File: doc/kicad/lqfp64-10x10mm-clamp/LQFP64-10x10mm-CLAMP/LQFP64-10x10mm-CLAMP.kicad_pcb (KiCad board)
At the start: 2 copper layers, 50 x 25 mm, 11 parts, among them J0 Conn_01x01, J1 Conn_01x16, J2 Conn_01x16, J3 Conn_01x16, J4 Conn_01x16, J5 Conn_01x12, J6 Conn_01x12, J7 Conn_01x12, J8 Conn_01x12, U1 LQFP64-G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

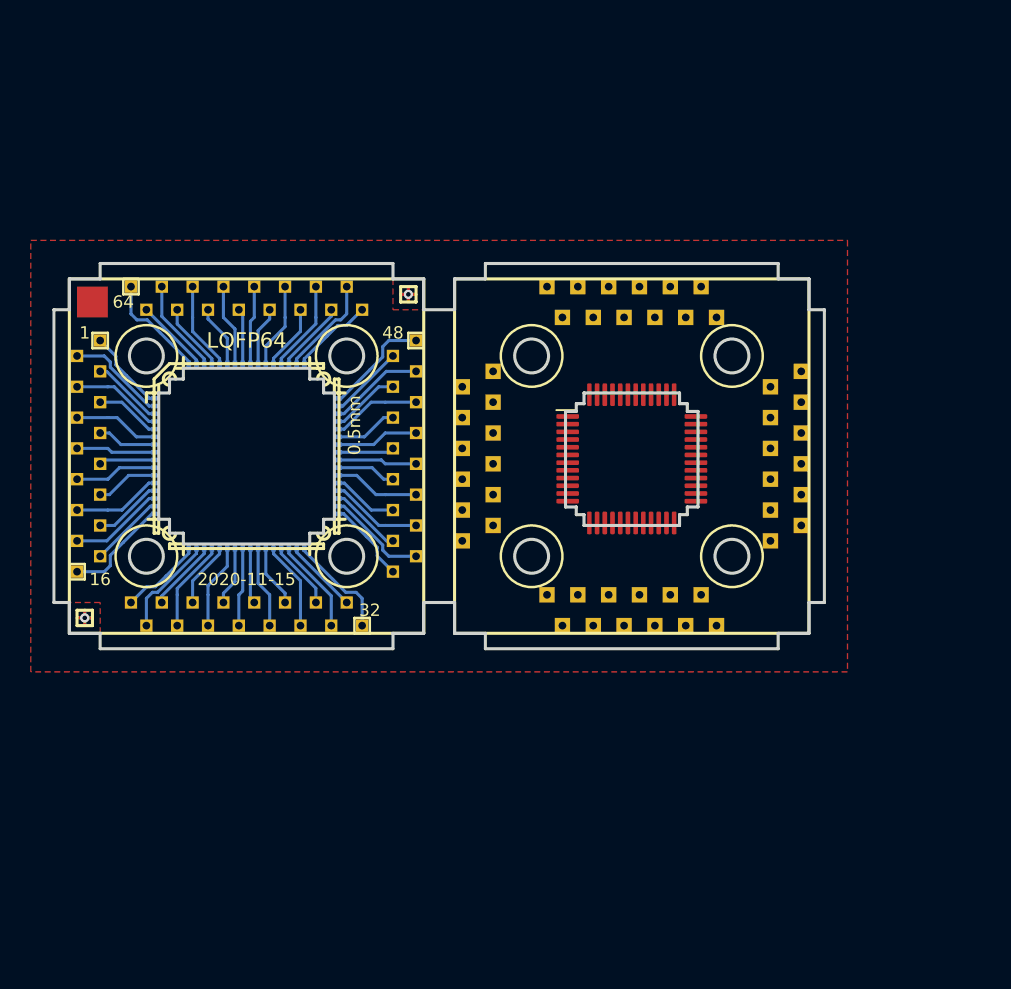
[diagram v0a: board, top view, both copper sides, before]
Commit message: doc/kicad: LQFP64-10x10mm-CLAMP bottom board
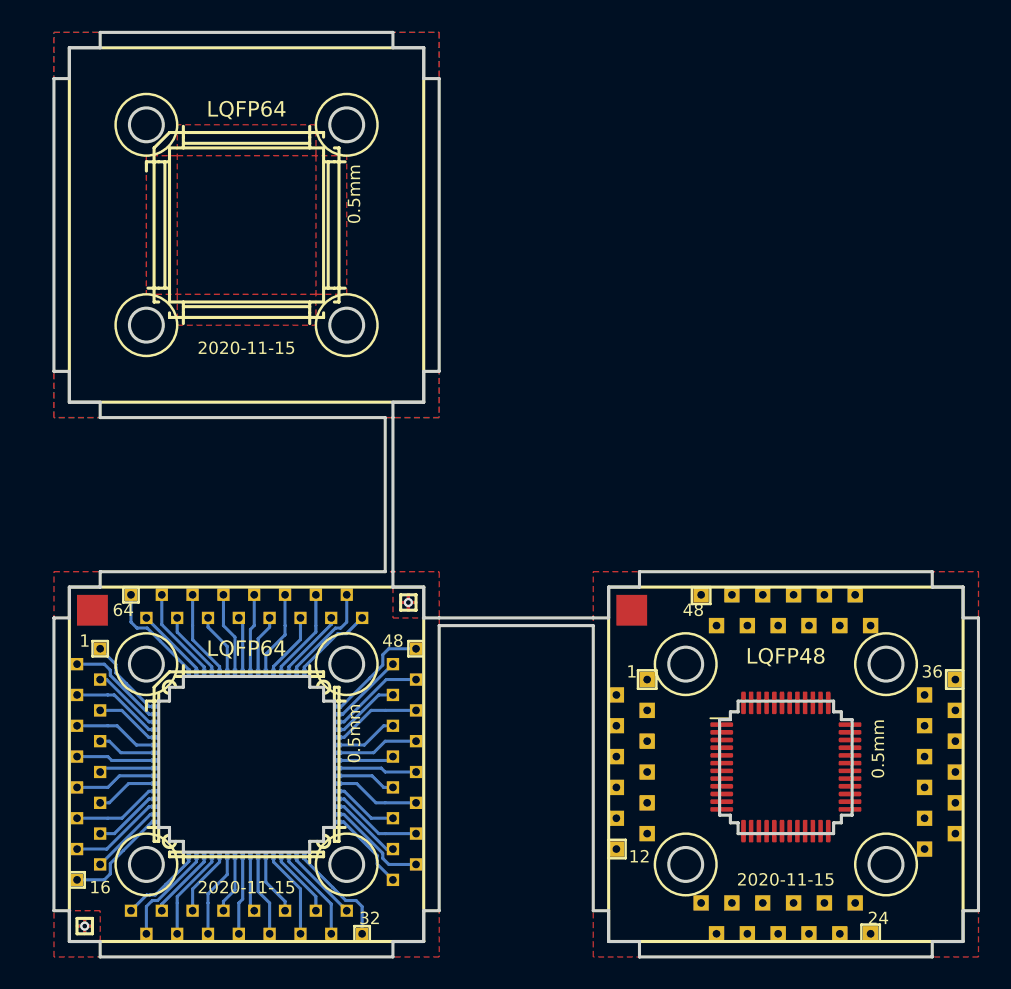
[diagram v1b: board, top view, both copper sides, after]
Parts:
- added J10: Conn_01x01, fmlibf:JS_2x2mm, F.Cu at (78.0, 67.0)
- added REF**: LQFP-64_10x10mm_P0.5mm_HS, fmlibf:LQFP-64_10x10mm_P0.5mm_HS, F.Cu at (53.0, 42.0)
- moved J5 22.4 mm to (78.0, 77.0)
- moved J6 22.4 mm to (88.0, 87.0)
- moved J7 22.4 mm to (98.0, 77.0)
- moved J8 22.4 mm to (88.0, 67.0)
- moved U2 22.4 mm to (88.0, 77.2)
- moved J0 20.0 mm to (43.0, 67.0)
- moved J1 20.0 mm to (43.0, 77.0)
- moved J2 20.0 mm to (53.0, 87.0)
- moved J3 20.0 mm to (63.0, 77.0)
- moved J4 20.0 mm to (53.0, 67.0)
- moved U1 20.0 mm to (53.0, 77.0)
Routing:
- added copper zone on B.Cu, net (none)
- added copper zone on F.Cu, net (none)
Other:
- board size 50 x 25 mm -> 60 x 60 mm
- board text added: "12"
- board text added: "24"
- board text added: "36"
- board text added: "LQFP48"

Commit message: doc/kicad: LQFP64-10x10mm-CLAMP wire
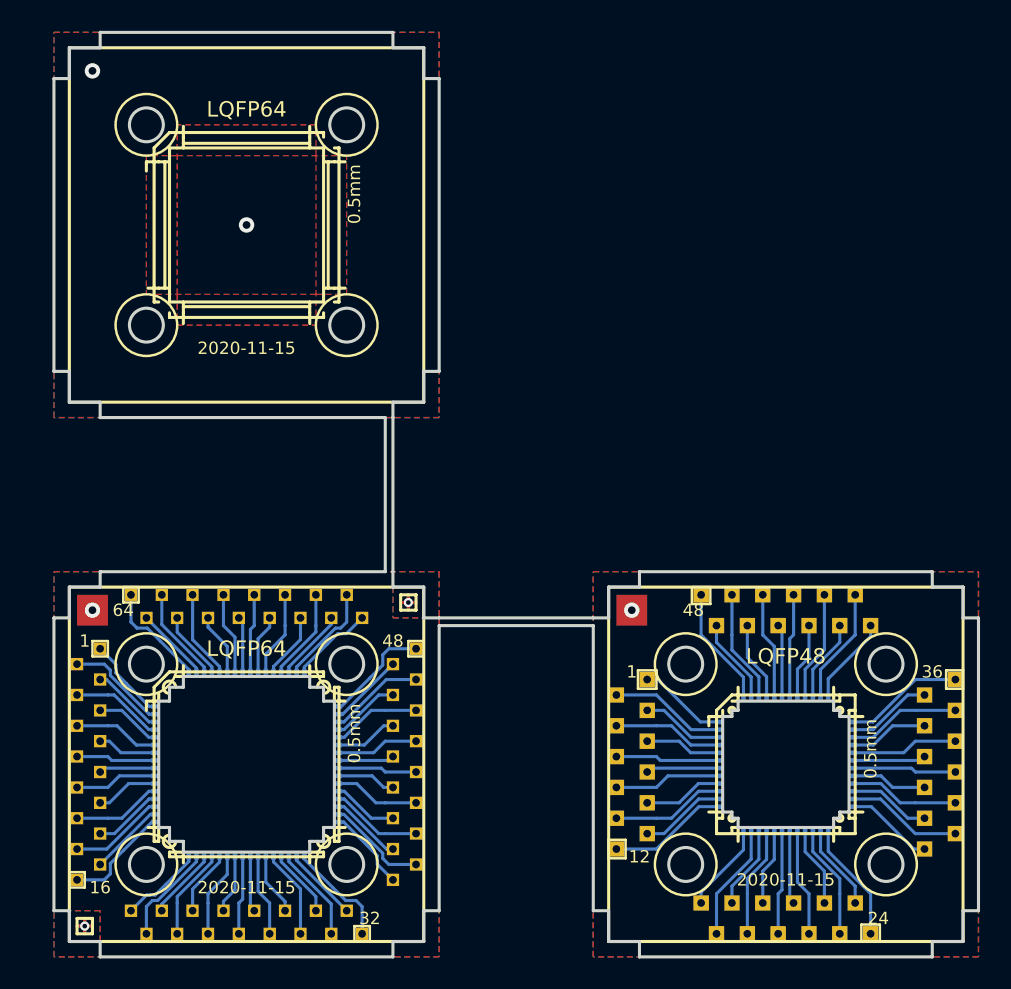
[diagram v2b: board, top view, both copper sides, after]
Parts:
- moved U2 0.18 mm to (88.0, 77.0)
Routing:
- net /P248: track 0.00 -> 7.64 mm
- net /P236: track 0.00 -> 7.64 mm
- net /P224: track 0.00 -> 7.64 mm
- net /P212: track 0.00 -> 7.64 mm
- net /P238: track 0.00 -> 7.47 mm
- net /P226: track 0.00 -> 7.47 mm
- net /P214: track 0.00 -> 7.47 mm
- net /P202: track 0.00 -> 7.47 mm
- net /P246: track 0.00 -> 7.26 mm
- net /P234: track 0.00 -> 7.26 mm
- net /P222: track 0.00 -> 7.26 mm
- net /P210: track 0.00 -> 7.26 mm
- net /P240: track 0.00 -> 7.06 mm
- net /P228: track 0.00 -> 7.06 mm
- net /P216: track 0.00 -> 7.06 mm
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- added copper zone on B.Cu, net GND
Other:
- outline, holes or cut-outs redrawn

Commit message: doc/kicad: LQFP64-10x10mm-CLAMP v0.1
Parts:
- added REF**: LQFP-48_7x7mm_P0.5mm_HS, fmlibf:LQFP-48_7x7mm_P0.5mm_HS, B.Cu at (53.0, 42.0)
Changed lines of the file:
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@@
   (general
     (thickness 1.6)
-    (drawings 278)
+    (drawings 280)
     (tracks 390)
     (zones 0)
-    (modules 13)
+    (modules 14)
     (nets 114)
   )
@@
     (add_net /P248)
     (add_net GND)
+  )
+  (module fmlibf:LQFP-48_7x7mm_P0.5mm_HS (layer B.Cu)
+    (at 53 42 180)
+    (descr "LQFP48 for LQFP64-10x10mm-CLAMP")
+    (tags "LQFP QFP")
+    (attr smd)
+    (fp_text reference REF** (at 0 5.85) (layer B.SilkS) hide
+      (effects (font (size 1 1) (thickness 0.15)) (justify mirror))
+    )
+    (fp_text value LQFP-48_7x7mm_P0.5mm_HS (at 0 -5.85) (layer B.Fab) hide
+      (effects (font (size 1 1) (thickness 0.15)) (justify mirror))
+    )
+    (fp_text user %R (at 0 0) (layer B.Fab) hide
+      (effects (font (size 1 1) (thickness 0.15)) (justify mirror))
+    )
+    (fp_line (start -4.5 -3.1) (end -4.5 3.1) (layer B.SilkS) (width 0.2))
+    (fp_line (start 3.1 -4.5) (end -3.1 -4.5) (layer B.SilkS) (width 0.2))
+    (fp_line (start 4.5 3.1) (end 4.5 -3.1) (layer B.SilkS) (width 0.2))
+    (fp_line (start -3.1 4.5) (end 3.1 4.5) (layer B.SilkS) (width 0.2))
+    (fp_line (start -4.5 -4.5) (end -4.5 -3.1) (layer B.SilkS) (width 0.2))
+    (fp_line (start -3.5 4.5) (end -3.1 4.5) (layer B.SilkS) (width 0.2))
+    (fp_line (start 4.5 4.5) (end 4.5 3.1) (layer B.SilkS) (width 0.2))
+    (fp_line (start 4.5 -4.5) (end 3.1 -4.5) (layer B.SilkS) (width 0.2))
+    (fp_line (start -5 3.1) (end -5 2.5) (layer B.SilkS) (width 0.2))
+    (fp_line (start -4.1 3.1) (end -5 3.1) (layer B.SilkS) (width 0.2))
+    (fp_line (start -4.1 -3.1) (end -5 -3.1) (layer B.SilkS) (width 0.2))
+    (fp_line (start 4.1 -3.1) (end 5 -3.1) (layer B.SilkS) (width 0.2))
+    (fp_line (start 3.1 -5) (end 3.1 -4.1) (layer B.SilkS) (width 0.2))
+    (fp_line (start -3.1 -4.1) (end -3.1 -5) (layer B.SilkS) (width 0.2))
+    (fp_line (start 4.1 3.1) (end 5 3.1) (layer B.SilkS) (width 0.2))
+    (fp_line (start 3.1 4.1) (end 3.1 5) (layer B.SilkS) (width 0.2))
+    (fp_line (start -3.1 4.1) (end -3.1 5) (layer B.SilkS) (width 0.2))
+    (fp_line (start -4.5 3.5) (end -3.5 4.5) (layer B.SilkS) (width 0.2))
+    (fp_line (start -4.5 3.1) (end -4.5 3.5) (layer B.SilkS) (width 0.2))
+    (fp_line (start -3.1 -4.5) (end -4.5 -4.5) (layer B.SilkS) (width 0.2))
+    (fp_line (start 4.5 -3.1) (end 4.5 -4.5) (layer B.SilkS) (width 0.2))
+    (fp_line (start 3.1 4.5) (end 4.5 4.5) (layer B.SilkS) (width 0.2))
+    (fp_line (start -3.5 3.5) (end 3.5 3.5) (layer B.SilkS) (width 0.2))
+    (fp_line (start 3.5 3.5) (end 3.5 -3.5) (layer B.SilkS) (width 0.2))
+    (fp_line (start 3.5 -3.5) (end -3.5 -3.5) (layer B.SilkS) (width 0.2))
+    (fp_line (start -3.5 -3.5) (end -3.5 3.5) (layer B.SilkS) (width 0.2))
+    (fp_line (start -3.1 4.1) (end -3.1 3.5) (layer B.SilkS) (width 0.2))
+    (fp_line (start 3.1 4.1) (end 3.1 3.5) (layer B.SilkS) (width 0.2))
+    (fp_line (start 4.1 3.1) (end 3.5 3.1) (layer B.SilkS) (width 0.2))
+    (fp_line (start 3.1 -4.1) (end 3.1 -3.5) (layer B.SilkS) (width 0.2))
+    (fp_line (start 4.1 -3.1) (end 3.5 -3.1) (layer B.SilkS) (width 0.2))
+    (fp_line (start -3.1 -4.1) (end -3.1 -3.5) (layer B.SilkS) (width 0.2))
+    (fp_line (start -4.1 -3.1) (end -3.5 -3.1) (layer B.SilkS) (width 0.2))
+    (fp_line (start -4.1 3.1) (end -3.5 3.1) (layer B.SilkS) (width 0.2))
+    (fp_line (start -3.1 3.9) (end 3.1 3.9) (layer B.SilkS) (width 0.2))
+    (fp_line (start 3.9 3.1) (end 3.9 -3.1) (layer B.SilkS) (width 0.2))
+    (fp_line (start 3.1 -3.9) (end -3.1 -3.9) (layer B.SilkS) (width 0.2))
+    (fp_line (start -3.9 -3.1) (end -3.9 3.1) (layer B.SilkS) (width 0.2))
   )
   (module fmlibf:LQFP-64_10x10mm_P0.5mm_HS (layer F.Cu)
@@
       (net 1 GND))
   )
+  (gr_text 0.5mm (at 47.5 41 270) (layer B.SilkS)
+    (effects (font (size 0.8 0.8) (thickness 0.15)) (justify mirror))
+  )
+  (gr_text LQFP48 (at 53 35) (layer B.SilkS)
+    (effects (font (size 1 1) (thickness 0.2)) (justify mirror))
+  )
   (gr_text P1 (at 82 74) (layer B.SilkS)
